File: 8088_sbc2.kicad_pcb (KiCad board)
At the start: 2 copper layers, 200 x 100 mm, 65 parts, among them P1 CONN_02X10, P2 JMP_USB_PWR, P3 USB_B, Q1 IRLML6402, SW1 SW_PUSH, U1 P8088, U11 74HC573, U12 74HC573, U13 74HC573, U14 74HC573, U15 74HC138, U16 74HC138, U17 74HC14_OWN, U18 74HC08, U19 74HC32, U2 28C64, U20 10xLEDBAR, U3 AS6C4008, U4 TL770xA, U5 16C550, U6 FT232RL, U7 OSC_SMALL

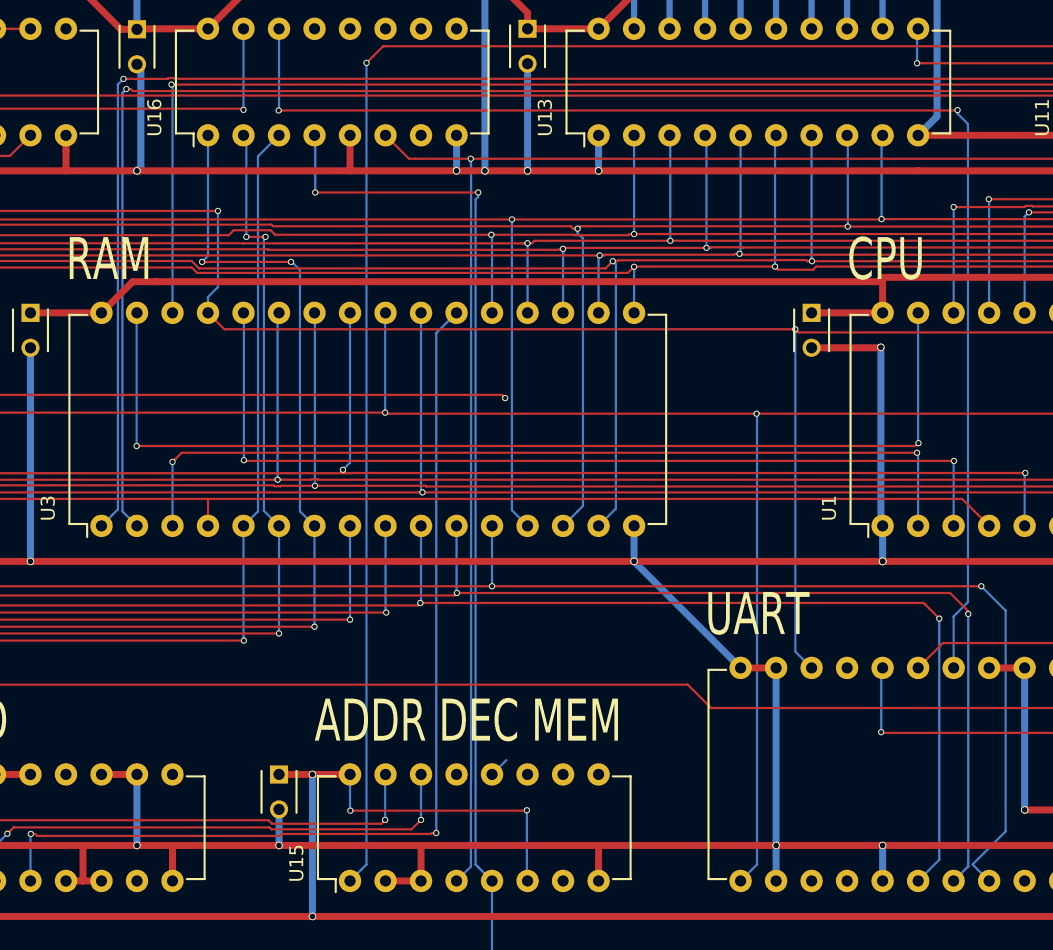
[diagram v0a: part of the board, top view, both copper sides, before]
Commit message: DRC w/ cheaper tolerances successful
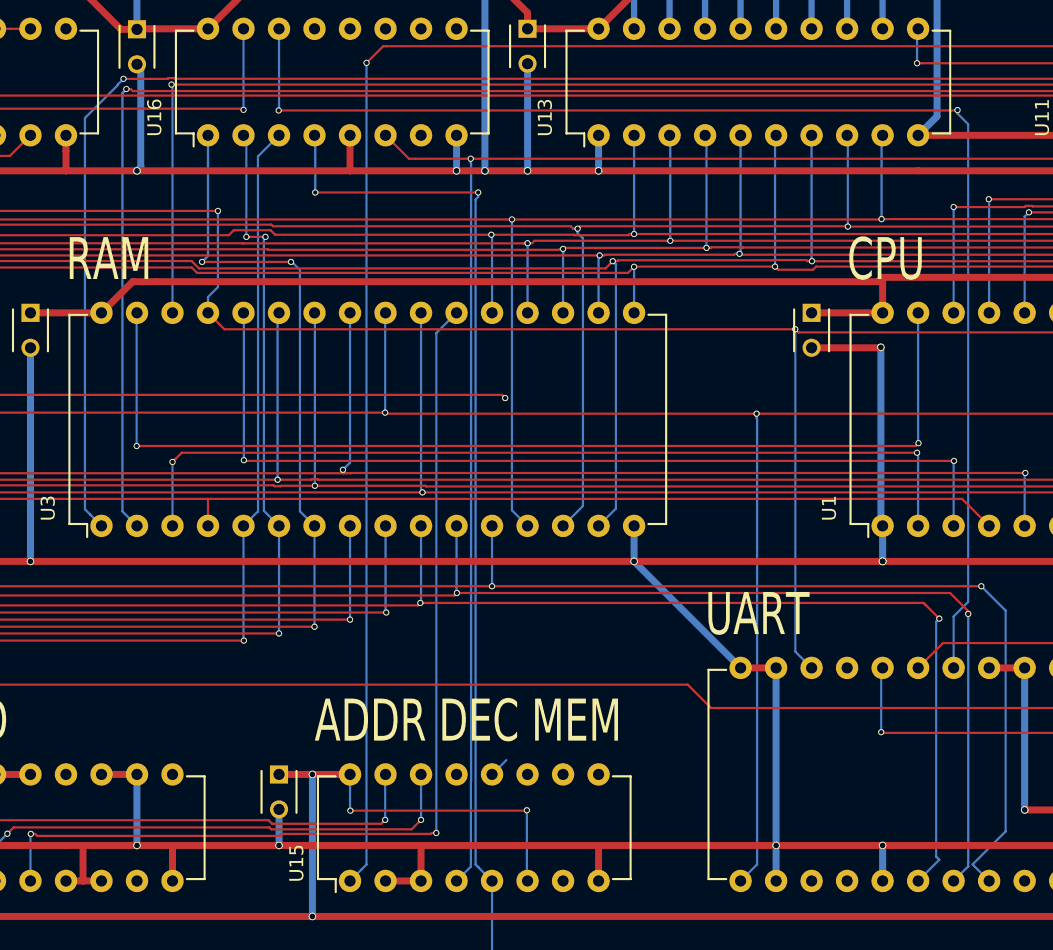
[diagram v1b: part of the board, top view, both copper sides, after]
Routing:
- net /A18: track 113.0 -> 114.0 mm
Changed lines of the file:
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@@
   (general
     (links 333)
-    (no_connects 5)
+    (no_connects 4)
     (area 42.267857 49.924999 257.732143 150.075001)
     (thickness 1.6)
     (drawings 28)
-    (tracks 1751)
+    (tracks 1757)
     (zones 0)
     (modules 65)
@@
   (via (at 93.2054 90.9956) (size 0.45) (drill 0.3) (layers F.Cu B.Cu) (net 72))
   (via (at 116.7512 90.9702) (size 0.45) (drill 0.3) (layers F.Cu B.Cu) (net 72))
+  (segment (start 155.283 105.4736) (end 155.283 105.791798) (width 0.16) (layer B.Cu) (net 73))
+  (segment (start 155.283 105.791798) (end 155.320001 105.828799) (width 0.16) (layer B.Cu) (net 73))
+  (segment (start 155.320001 105.828799) (end 155.320001 137.719999) (width 0.16) (layer B.Cu) (net 73))
+  (segment (start 155.320001 137.719999) (end 155.315001 137.724999) (width 0.16) (layer B.Cu) (net 73))
   (segment (start 128.7146 105.3974) (end 100.8 105.3974) (width 0.16) (layer F.Cu) (net 73))
   (segment (start 100.8 105.3974) (end 75.4508 105.3974) (width 0.16) (layer F.Cu) (net 73))
@@
   (segment (start 155.283 105.4736) (end 128.7908 105.4736) (width 0.16) (layer F.Cu) (net 73))
   (segment (start 154.14 138.9) (end 155.315001 137.724999) (width 0.16) (layer B.Cu) (net 73))
-  (segment (start 155.315001 137.724999) (end 155.315001 105.505601) (width 0.16) (layer B.Cu) (net 73))
   (via (at 155.283 105.4736) (size 0.45) (drill 0.3) (layers F.Cu B.Cu) (net 73))
   (segment (start 128.7146 105.3974) (end 128.7146 98.2854) (width 0.16) (layer B.Cu) (net 73))
@@
   (via (at 128.7908 119.6976) (size 0.45) (drill 0.3) (layers F.Cu B.Cu) (net 84))
   (segment (start 76.199999 114.299999) (end 75.4 113.5) (width 0.16) (layer B.Cu) (net 84))
+  (segment (start 168.354999 137.385001) (end 168.13 137.160002) (width 0.16) (layer B.Cu) (net 85))
+  (segment (start 168.13 137.160002) (end 168.13 120.3565) (width 0.16) (layer B.Cu) (net 85))
+  (segment (start 168.13 120.3565) (end 168.354999 120.131501) (width 0.16) (layer B.Cu) (net 85))
   (segment (start 167.362298 119.1388) (end 168.354999 120.131501) (width 0.16) (layer F.Cu) (net 85))
   (segment (start 167.2972 119.073702) (end 167.362298 119.1388) (width 0.16) (layer F.Cu) (net 85))
@@
   (segment (start 78.980001 119.522798) (end 78.965001 119.507798) (width 0.16) (layer B.Cu) (net 85))
   (segment (start 78.965001 119.507798) (end 78.965001 119.1896) (width 0.16) (layer B.Cu) (net 85))
-  (segment (start 168.354999 137.385001) (end 168.354999 120.131501) (width 0.16) (layer B.Cu) (net 85))
   (segment (start 166.84 138.9) (end 168.354999 137.385001) (width 0.16) (layer B.Cu) (net 85))
   (segment (start 78.965001 119.1896) (end 78.965001 114.525001) (width 0.16) (layer B.Cu) (net 85))
@@
   (segment (start 78.965001 114.525001) (end 78.739999 114.299999) (width 0.16) (layer B.Cu) (net 85))
   (segment (start 78.739999 114.299999) (end 77.94 113.5) (width 0.16) (layer B.Cu) (net 85))
-  (segment (start 169.38 138.9) (end 170.423719 137.856281) (width 0.16) (layer B.Cu) (net 86))
-  (segment (start 170.423719 137.856281) (end 170.42485 137.85515) (width 0.16) (layer B.Cu) (net 86))
   (segment (start 170.42485 119.7992) (end 170.42485 137.58025) (width 0.16) (layer B.Cu) (net 86))
   (segment (start 170.42485 137.58025) (end 170.418822 137.586278) (width 0.16) (layer B.Cu) (net 86))
+  (segment (start 169.38 138.9) (end 170.423719 137.856281) (width 0.16) (layer B.Cu) (net 86))
+  (segment (start 170.423719 137.856281) (end 170.42485 137.85515) (width 0.16) (layer B.Cu) (net 86))
   (segment (start 170.418822 137.586278) (end 170.418822 137.851384) (width 0.16) (layer B.Cu) (net 86))
   (segment (start 170.418822 137.851384) (end 170.423719 137.856281) (width 0.16) (layer B.Cu) (net 86))
@@
   (segment (start 137.385001 104.441201) (end 137.2998 104.356) (width 0.16) (layer B.Cu) (net 88))
   (via (at 137.2998 104.356) (size 0.45) (drill 0.3) (layers F.Cu B.Cu) (net 88))
+  (segment (start 109.595001 81.959801) (end 107.239999 84.314803) (width 0.16) (layer B.Cu) (net 89))
+  (segment (start 107.239999 84.314803) (end 107.239999 112.319999) (width 0.16) (layer B.Cu) (net 89))
+  (segment (start 107.239999 112.319999) (end 107.620001 112.700001) (width 0.16) (layer B.Cu) (net 89))
+  (segment (start 107.620001 112.700001) (end 108.42 113.5) (width 0.16) (layer B.Cu) (net 89))
   (via (at 109.9948 81.5214) (size 0.45) (drill 0.3) (layers F.Cu B.Cu) (net 89))
   (segment (start 109.9948 81.5214) (end 113.152148 81.5214) (width 0.16) (layer F.Cu) (net 89))
@@
   (segment (start 187.16 80.79591) (end 187.1679 80.80381) (width 0.16) (layer B.Cu) (net 89))
   (segment (start 187.16 77.94) (end 187.16 80.79591) (width 0.16) (layer B.Cu) (net 89))
-  (segment (start 109.595001 81.959801) (end 109.595001 112.324999) (width 0.16) (layer B.Cu) (net 89))
-  (segment (start 109.595001 112.324999) (end 109.219999 112.700001) (width 0.16) (layer B.Cu) (net 89))
-  (segment (start 109.219999 112.700001) (end 108.42 113.5) (width 0.16) (layer B.Cu) (net 89))
   (segment (start 110.198 82.25019) (end 110.516198 82.25019) (width 0.16) (layer F.Cu) (net 90))
   (segment (start 110.516198 82.25019) (end 110.661197 82.395189) (width 0.16) (layer F.Cu) (net 90))
@@
   (segment (start 177.0635 123.7235) (end 177 123.66) (width 0.16) (layer B.Cu) (net 95))
   (segment (start 220.8032 70.8604) (end 222.8794 70.8604) (width 0.16) (layer F.Cu) (net 95))
-  (segment (start 170.405001 118.951999) (end 169.38 119.977) (width 0.16) (layer B.Cu) (net 96))
-  (segment (start 169.38 119.977) (end 169.38 123.66) (width 0.16) (layer B.Cu) (net 96))
-  (segment (start 169.6594 83.7566) (end 169.6594 84.004087) (width 0.16) (layer B.Cu) (net 96))
-  (segment (start 169.6594 84.004087) (end 170.405001 84.749688) (width 0.16) (layer B.Cu) (net 96))
-  (segment (start 170.405001 84.749688) (end 170.405001 118.951999) (width 0.16) (layer B.Cu) (net 96))
+  (segment (start 169.38 123.66) (end 169.38 119.977) (width 0.16) (layer B.Cu) (net 96))
+  (segment (start 169.38 119.977) (end 170.420001 118.936999) (width 0.16) (layer B.Cu) (net 96))
+  (segment (start 170.420001 118.936999) (end 170.420001 84.764688) (width 0.16) (layer B.Cu) (net 96))
+  (segment (start 170.420001 84.764688) (end 169.6594 84.004087) (width 0.16) (layer B.Cu) (net 96))
+  (segment (start 169.6594 84.004087) (end 169.6594 83.7566) (width 0.16) (layer B.Cu) (net 96))
   (segment (start 121.0946 83.782) (end 169.634 83.782) (width 0.16) (layer F.Cu) (net 96))
   (segment (start 169.634 83.782) (end 169.6594 83.7566) (width 0.16) (layer F.Cu) (net 96))

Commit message: weiter
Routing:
- net Net-(U5-Pad10): track 51.8 -> 101.6 mm, vias 3 -> 2
- net /nROMEN: track 64.4 -> 89.7 mm, vias 2 -> 1
- net /D1: track 220.4 -> 240.8 mm
- net /IODEV0_WREN: track 97.7 -> 112.4 mm, vias 4 -> 3
- net GND: track 1059.6 -> 1068.4 mm, vias 19 -> 14
- net /nIODEV0_WREN: track 166.4 -> 164.1 mm
- net Net-(U5-Pad37): track 103.0 -> 102.0 mm, vias 3 -> 2
- net /A8: track 141.3 -> 140.4 mm, vias 3 -> 2
- net /CLK: track 136.7 -> 135.9 mm
- net /D0: track 232.6 -> 233.4 mm, vias 6 -> 5
- net /nRD: track 184.5 -> 184.0 mm, vias 5 -> 4
- net VCC: track 833.5 -> 833.7 mm, vias 21 -> 19
- net /A11: vias 3 -> 2

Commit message: almost ready for submission
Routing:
- net VCC: track 833.7 -> 814.8 mm, vias 19 -> 16
- net /IODEV0_WREN: track 112.4 -> 101.5 mm
- net Net-(U5-Pad10): track 101.6 -> 98.8 mm
- net /D4: track 218.6 -> 220.8 mm, vias 6 -> 5
- added copper zone on B.Cu, net GND
- added copper zone on F.Cu, net GND
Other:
- outline, holes or cut-outs redrawn
